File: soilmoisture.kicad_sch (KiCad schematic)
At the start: 13 parts, among them J1 Conn_ARM_JTAG_SWD_10, U1 BT840, U2 BAT-HLD-001, Y1 ABS07-32.768KHZ-T

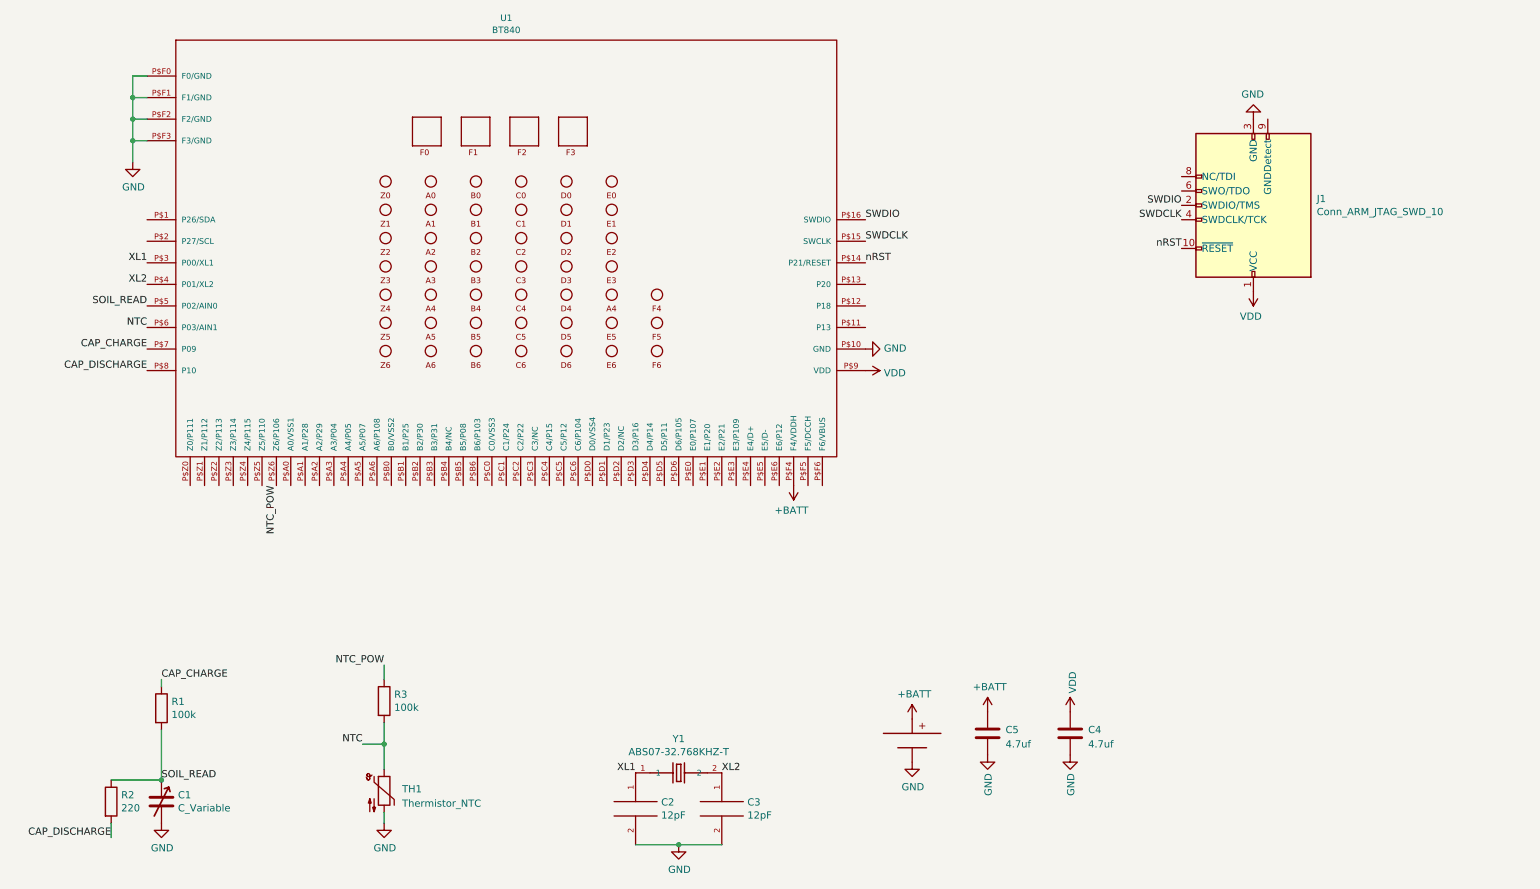
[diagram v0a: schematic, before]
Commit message: Feat: Memsic oscillator and schmitt buffer, dual probes
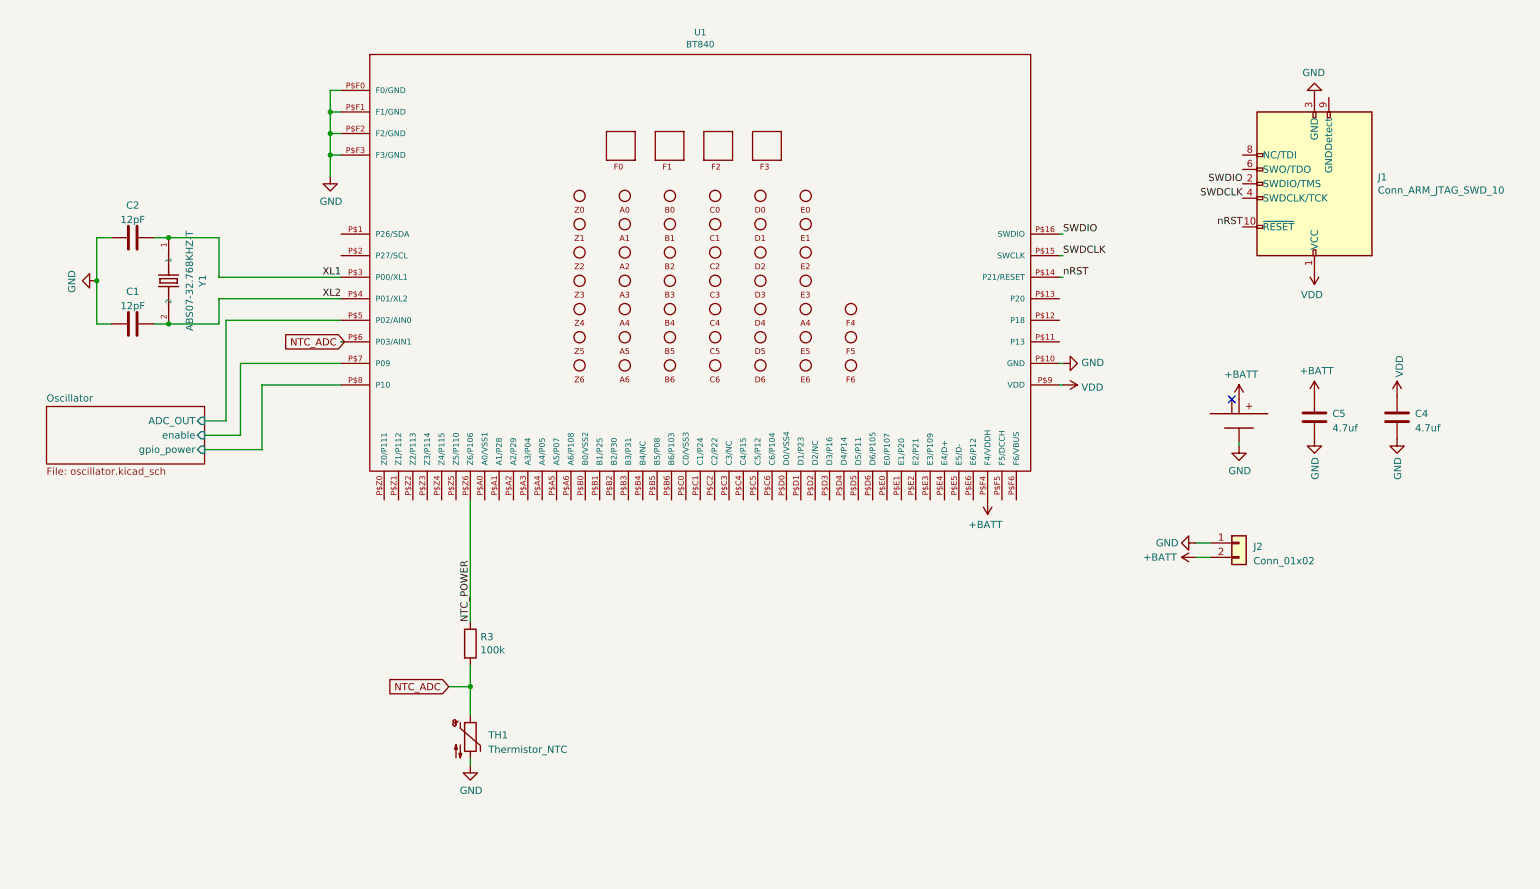
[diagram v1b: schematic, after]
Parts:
- removed C1: C_Variable, Capacitor_SMD:C_0603_1608Metric, symbol Device:C_Variable
- removed C2, C3: 12pF, Capacitor_SMD:C_0603_1608Metric, symbol soilmoisture-rescue:CAP-pspice
- removed R1: 100k, Resistor_SMD:R_0603_1608Metric, symbol Device:R
- removed R2: 220, Resistor_SMD:R_0603_1608Metric, symbol Device:R
- added C1, C2: 12pF, Capacitor_SMD:C_0603_1608Metric, symbol Device:C
- added J2: Conn_01x02, Connector_PinHeader_2.54mm:PinHeader_1x02_P2.54mm_Vertical, symbol Connector_Generic:Conn_01x02
- U2: footprint BAT-HLD-001:BAT-HLD-001 -> BAT-HLD-001
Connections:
- net +BATT: now also J2.2 (Pin_2); no longer U2.+@1
- net GND: now also C1.1, C2.1, J2.1 (Pin_1)
- net XL1: now also C2.2
- net XL2: now also C1.2
- net CAP_CHARGE renamed Oscillator/enable
- net CAP_DISCHARGE renamed Oscillator/gpio_power
- net NTC renamed NTC_ADC
- net NTC_POW renamed NTC_POWER
- net SOIL_READ renamed Oscillator/ADC_OUT
- no-connect marks 0 -> 1
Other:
- added sheet Oscillator (oscillator.kicad_sch)
- moved on the sheet: C4, C5, J1, R3, TH1, U1, Y1
